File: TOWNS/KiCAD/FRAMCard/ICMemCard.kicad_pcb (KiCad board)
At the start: 2 copper layers, 79.1 x 50.5 mm, 19 parts, among them J1 PCMCIA_Connector, Q1 BC846X, Q2 BC846X, U1 FM18W08-SGTR, U2 FM18W08-SGTR, U3 74AHCT1G32

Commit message: Working on PCB for NX1 PCMCIA frame.
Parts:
- removed the REF** at (139.1, 99.9)
- removed the REF** at (139.1, 51.9)
- added REF**: MountingHole_1.5mm, MountingHole:MountingHole_2.1mm, F.Cu at (68.5, 59.3)
- added REF**: MountingHole_1.5mm, MountingHole:MountingHole_2.1mm, F.Cu at (59.3, 92.8)
- moved U1 9.38 mm to (102.1, 81.2)
- moved D1 8.41 mm to (66.5, 66.3), turned to 90 degrees
- moved D2 6.64 mm to (66.5, 71.6), turned to 90 degrees
- moved U2 2.57 mm to (109.9, 63.3)
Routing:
- net /A12: track 54.1 -> 75.8 mm
- net GND: track 555.9 -> 538.5 mm, vias 3 -> 4
- net Vcc: track 282.4 -> 270.0 mm
- net /A6: track 70.7 -> 59.8 mm, vias 0 -> 2
- net /D0: track 39.5 -> 49.6 mm
- net /D1: track 41.6 -> 51.7 mm
- net Net-(D1-Pad1): track 18.6 -> 28.6 mm
- net /D7: track 62.5 -> 72.5 mm
- net /~WE~orWP: track 130.8 -> 140.5 mm
- net /A11: track 82.5 -> 92.0 mm
- net /D2: track 44.8 -> 54.4 mm
- net /D6: track 66.0 -> 75.2 mm
- net /D5: track 70.0 -> 79.1 mm
- net /~OE: track 132.8 -> 141.9 mm
- net /D4: track 74.2 -> 83.0 mm
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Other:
- board size 79.1 x 50.5 mm -> 78.5 x 47.2 mm
- board text added: "FM TOWNS RESCUE BOOT MEMORY CARD Using HIROSE NX1 PCMCIA FRAME by Captain YS http://www.ysflight.com Ver. 20220514"
- board text added: "PCMCIA Connector"
- board text removed: "FM TOWNS RESCUE BOOT MEMORY CARD by Captain YS http://www.ysflight.com Ver. 20220514"
- board text removed: "PCMCIA Connector 95622-003LF"

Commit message: Working on PCB for NX1 PCMCIA frame.
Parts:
- moved U3 11.5 mm to (74.7, 87.8), turned to 270 degrees
- moved REF** 9.12 mm to (68.5, 92.5)
- moved JP1 7.12 mm to (65.5, 84.1)
- moved C1 6.03 mm to (86.4, 89.9)
- moved D1 0.83 mm to (65.7, 66.3)
- moved D2 0.83 mm to (65.7, 71.6)
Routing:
- net GND: track 538.5 -> 377.2 mm
- net Vcc: track 270.0 -> 234.6 mm
- net /Wp: track 95.4 -> 83.6 mm
- net /~WE~orWP: track 140.5 -> 136.2 mm
- net /~WE: track 73.6 -> 75.6 mm
- net Net-(D1-Pad2): track 12.3 -> 14.3 mm
- net Net-(D2-Pad1): track 29.3 -> 31.2 mm
- net /D8: track 91.6 -> 90.1 mm
- net /D9: track 91.4 -> 90.0 mm
- net Net-(D1-Pad1): track 28.6 -> 29.9 mm
- net /D4: track 83.0 -> 81.9 mm
- net /D10: track 90.8 -> 89.8 mm
- net /A4: track 70.2 -> 69.3 mm
- net Net-(D2-Pad2): track 10.8 -> 11.6 mm
- net /D5: track 79.1 -> 78.3 mm
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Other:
- board text added: "Mounting Hole 2.1mm X 4.1mm Oval"
- board text removed: "Write_Unprotect"

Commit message: Working on PCB for NX1 PCMCIA frame.
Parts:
- moved D1 1.33 mm to (64.4, 66.3)
- moved D2 1.33 mm to (64.4, 71.6)
- moved U3 0.18 mm to (74.7, 87.6)
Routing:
- net Vcc: track 234.6 -> 212.6 mm, vias 4 -> 6
- net Net-(D2-Pad1): track 31.2 -> 35.4 mm
- net Net-(D1-Pad2): track 14.3 -> 16.6 mm
- net Net-(D2-Pad2): track 11.6 -> 13.8 mm
- net Net-(D1-Pad1): track 29.9 -> 29.5 mm, vias 0 -> 2

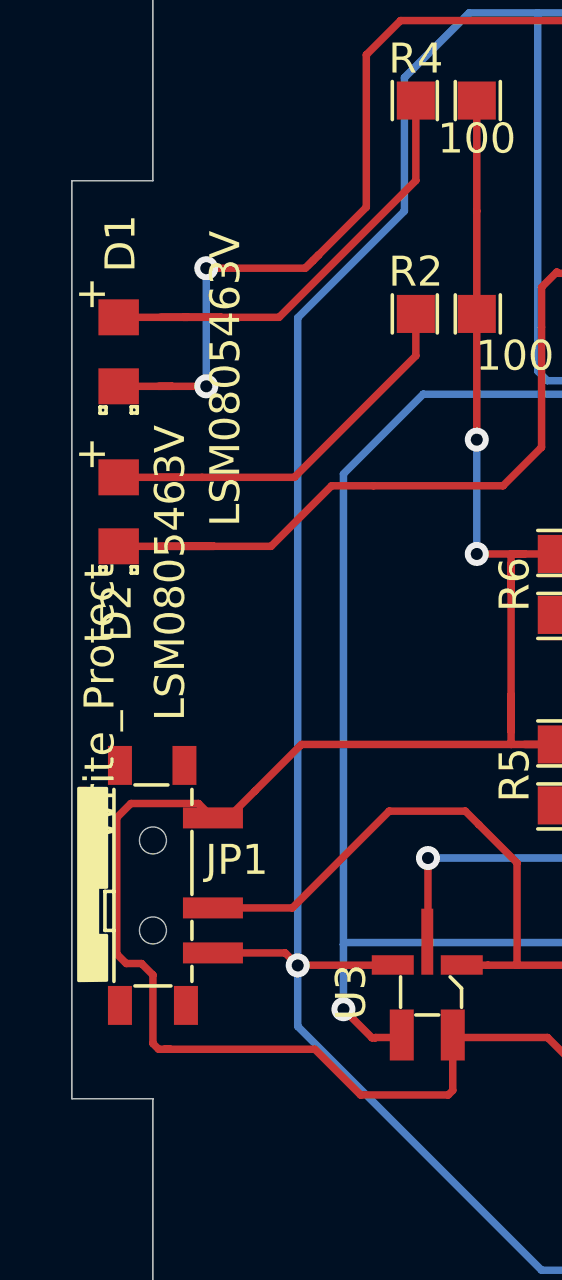
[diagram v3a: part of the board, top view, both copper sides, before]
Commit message: Added fillet
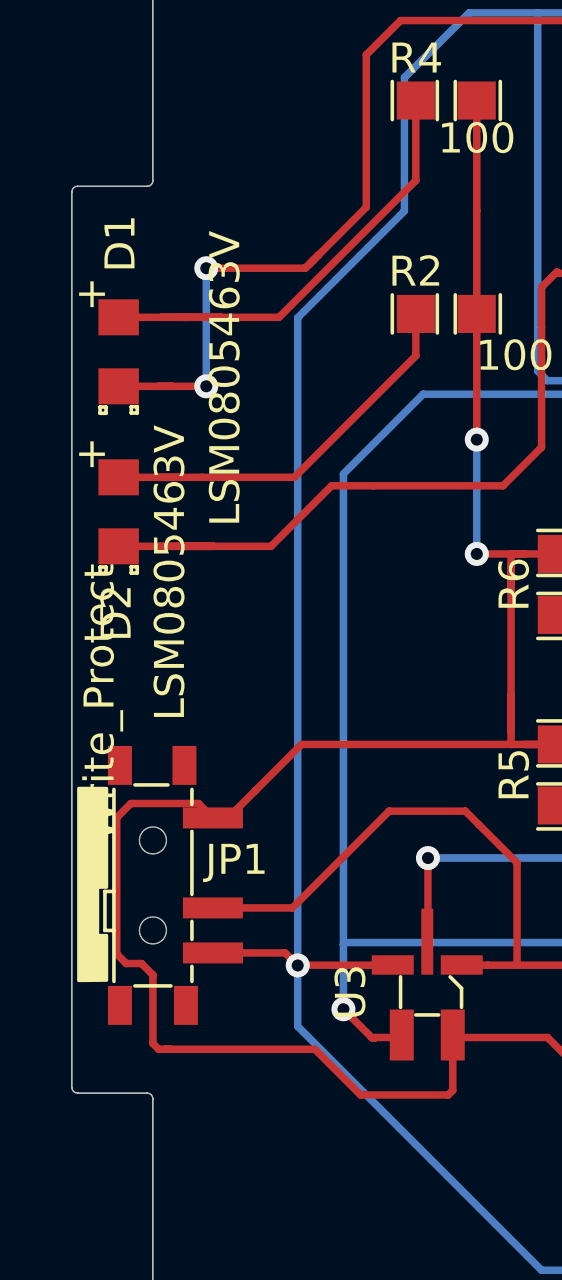
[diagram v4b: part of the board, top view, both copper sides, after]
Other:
- outline, holes or cut-outs redrawn

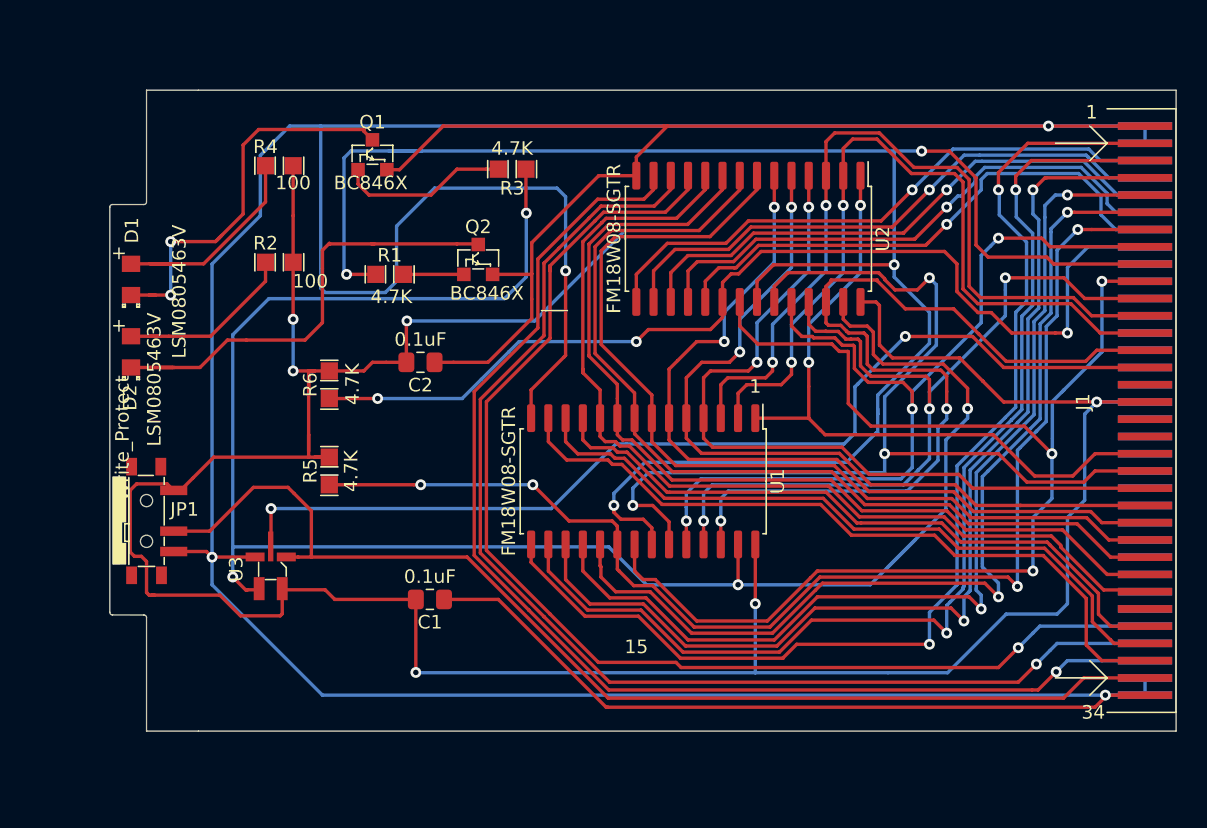
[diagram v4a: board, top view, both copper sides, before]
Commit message: Use 74LS32 instead of 1-CH OR gate.  Easier soldering.
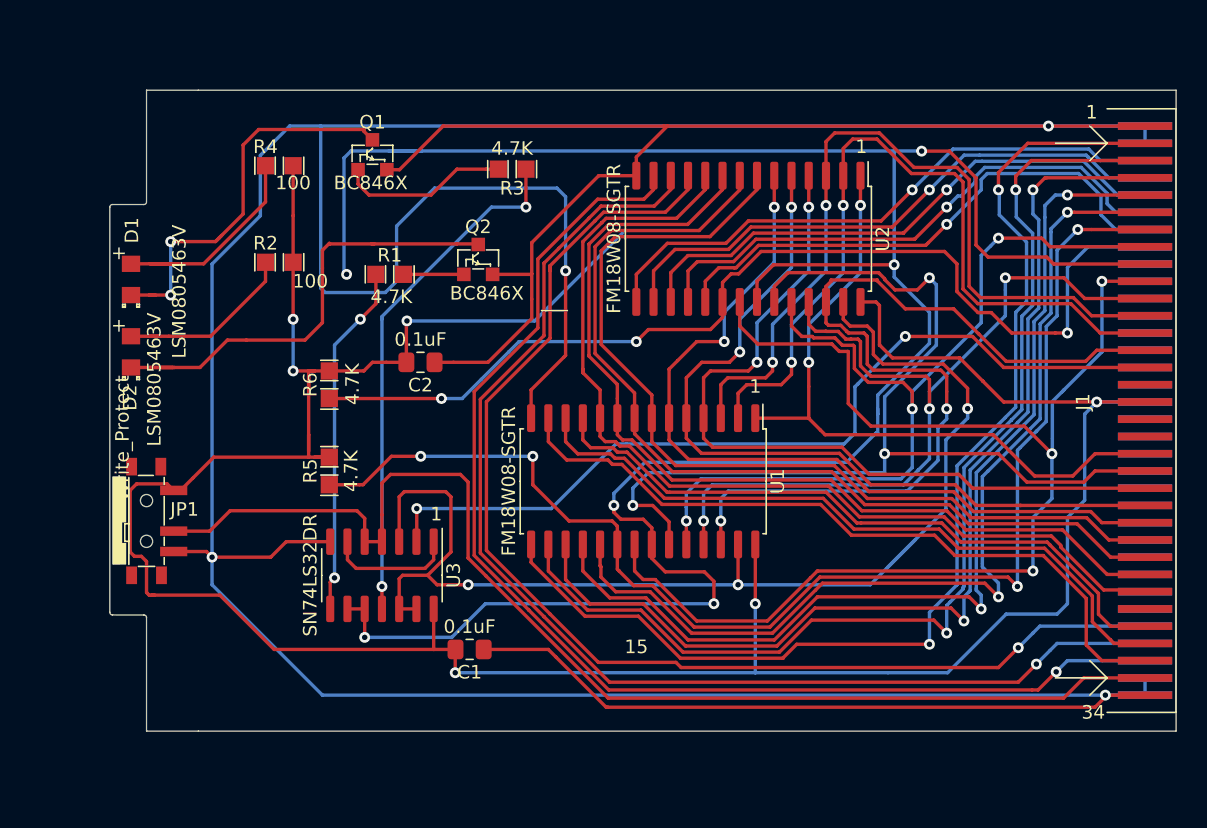
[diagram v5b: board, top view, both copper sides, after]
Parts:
- U3: value 74AHCT1G32 -> SN74LS32DR; footprint PCMCIA:SOT353_Easy -> Package_SO:SOIC-14_3.9x8.7mm_P1.27mm
- moved U3 8.20 mm to (82.9, 88.1)
- moved C1 4.70 mm to (89.3, 93.5)
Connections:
- R1 pad 2: /~OE -> Net-(R1-Pad2)
- R3 pad 2: /~WE~orWP -> Net-(R3-Pad2)
- U3 pad 1: /Wp -> /WPorWP
- U3 pad 3: GND -> /~WE~orWP
- U3 pad 4: /~WE~orWP -> /Wp
- U3 pad 5: Vcc -> /Wp
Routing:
- net /~WE~orWP: track 136.5 -> 89.3 mm, vias 4 -> 3
- net Net-(R3-Pad2): track 0.00 -> 38.3 mm, vias 0 -> 2
- net /~OE: track 141.9 -> 177.8 mm, vias 4 -> 6
- net Net-(R1-Pad2): track 0.00 -> 26.0 mm, vias 0 -> 2
- net /~WE: track 75.6 -> 64.3 mm
- net /WPorWP: track 0.00 -> 9.54 mm
- net /Wp: track 84.0 -> 89.4 mm
- net /~CE1: track 91.8 -> 94.7 mm
- net Vcc: track 212.6 -> 210.8 mm
- net GND: track 377.2 -> 378.6 mm

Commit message: Cleaning up PCB
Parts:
- JP1: value Write_Protect -> WP
- moved R5 2.67 mm to (74.4, 80.4)
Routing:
- net /~OE: track 177.8 -> 117.3 mm, vias 6 -> 5
- net Vcc: track 210.8 -> 204.9 mm
- net /~CE1: track 94.7 -> 99.6 mm
- net /Wp: track 89.4 -> 87.1 mm
- net /A11: track 92.0 -> 94.0 mm
- net /D7: track 72.5 -> 74.4 mm
- net /D6: track 74.7 -> 76.5 mm
- net /D5: track 78.3 -> 79.4 mm
- net /D3: track 84.3 -> 85.3 mm
- net /D4: track 81.9 -> 83.0 mm
- net /~WE~orWP: track 89.3 -> 88.3 mm
- net /D9: track 90.0 -> 89.3 mm
- net /D10: track 89.8 -> 89.3 mm
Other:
- board text added: "FM TOWNS RESCUE BOOT MEMORY CARD Using HIROSE NX1 PCMCIA FRAME by Captain YS http://www.ysflight.com Ver. 20220520"
- board text removed: "FM TOWNS RESCUE BOOT MEMORY CARD Using HIROSE NX1 PCMCIA FRAME by Captain YS http://www.ysflight.com Ver. 20220514"

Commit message: Cleaning up PCB
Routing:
- net GND: track 378.2 -> 347.4 mm
- net /~OE: track 117.3 -> 103.5 mm
- net /A14: track 68.0 -> 65.4 mm
- net /D11: track 43.7 -> 45.7 mm
- net /D12: track 42.7 -> 44.6 mm
- net /A9: track 63.5 -> 61.9 mm
- net /D13: track 41.5 -> 43.1 mm
- net /~WE~orWP: track 88.3 -> 87.2 mm
- net /D14: track 41.1 -> 42.2 mm
- net /A10: track 66.7 -> 65.7 mm
- net /A12: track 75.6 -> 74.6 mm
- net /A8: track 59.2 -> 59.7 mm
- net /A13: track 57.6 -> 58.1 mm

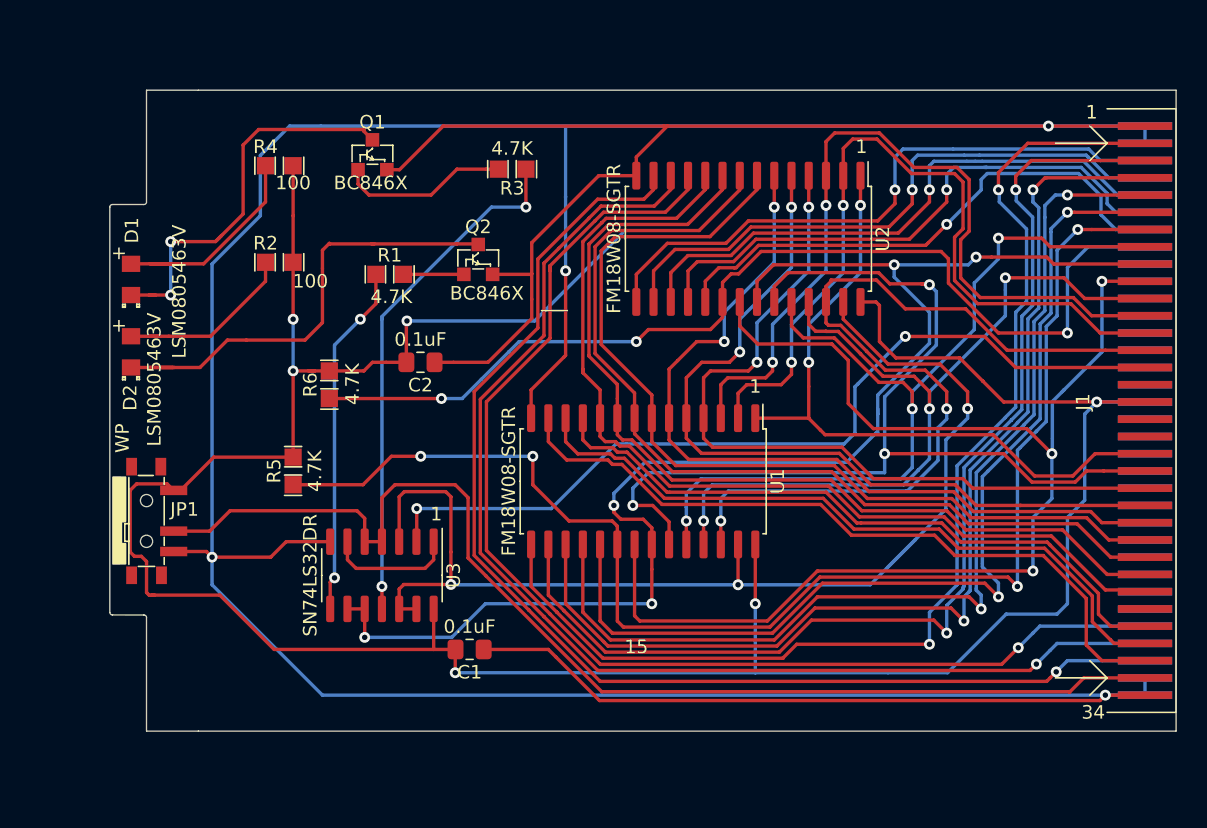
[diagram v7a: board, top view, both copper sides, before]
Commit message: Updating PCB bare version.
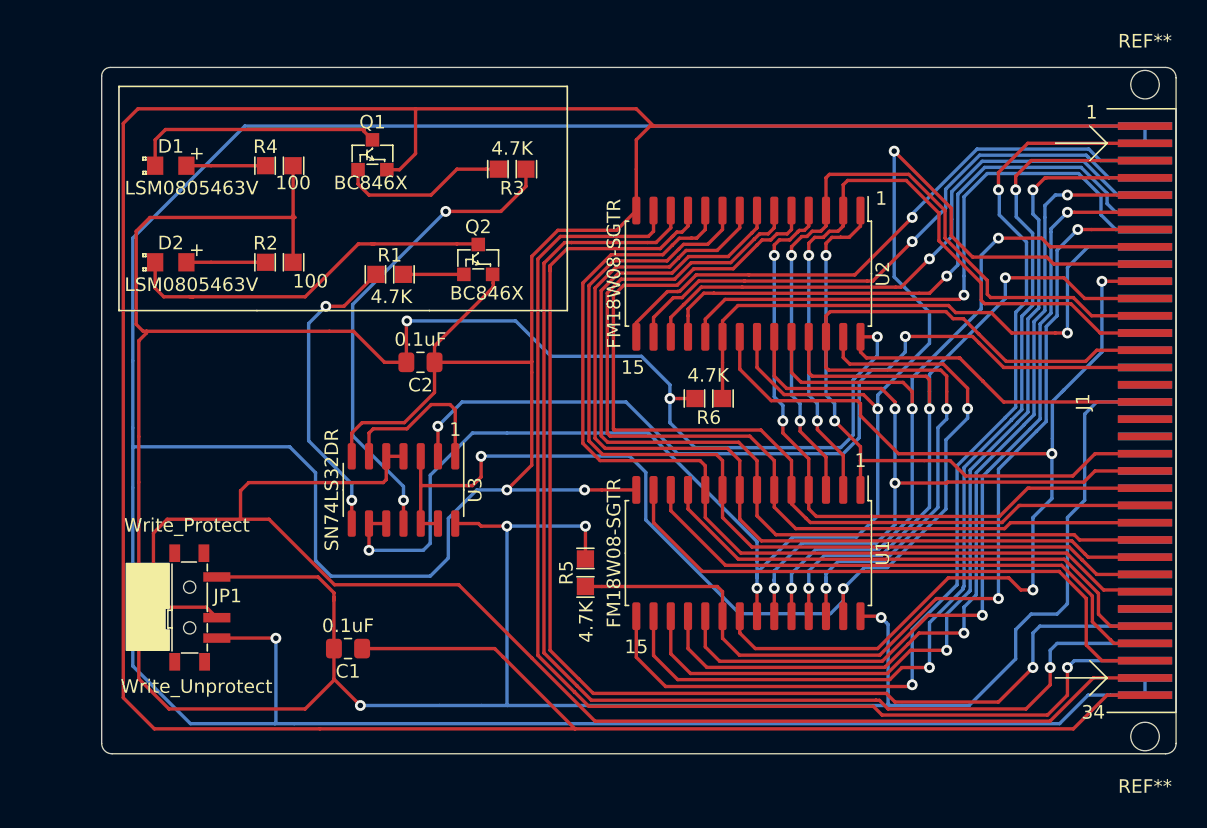
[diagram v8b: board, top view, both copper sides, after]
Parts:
- removed the REF** at (68.5, 59.3)
- removed the REF** at (68.5, 92.5)
- added REF**: MountingHole_1.5mm, MountingHole:MountingHole_2.1mm, F.Cu at (139.1, 99.9)
- added REF**: MountingHole_1.5mm, MountingHole:MountingHole_2.1mm, F.Cu at (139.1, 51.9)
- JP1: value WP -> Write_Protect
- moved R6 30.0 mm to (106.9, 77.0), turned to 180 degrees
- moved R5 22.8 mm to (95.9, 87.9)
- moved U1 9.38 mm to (109.9, 86.4)
- moved C1 8.95 mm to (80.4, 93.5)
- moved D1 8.87 mm to (67.3, 57.9), turned to 0 degrees
- moved D2 7.22 mm to (67.3, 65.0), turned to 0 degrees
- moved JP1 7.12 mm to (68.7, 90.4)
- moved U3 6.48 mm to (84.5, 81.8)
- moved U2 2.57 mm to (109.9, 65.9)
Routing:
- net GND: track 347.4 -> 529.5 mm, vias 4 -> 3
- net Vcc: track 204.8 -> 293.6 mm, vias 6 -> 7
- net /~CE2: track 75.1 -> 43.6 mm, vias 3 -> 1
- net /~CE1: track 99.6 -> 70.8 mm, vias 4 -> 2
- net /A12: track 74.6 -> 54.1 mm
- net /Wp: track 87.1 -> 106.9 mm
- net /~OE: track 103.5 -> 123.2 mm, vias 5 -> 4
- net /D7: track 74.4 -> 62.5 mm
- net /A11: track 93.6 -> 82.5 mm
- net /A6: track 59.7 -> 70.7 mm, vias 2 -> 0
- net Net-(D1-Pad1): track 29.5 -> 18.6 mm, vias 2 -> 0
- net Net-(D1-Pad2): track 16.6 -> 5.83 mm
- net /D6: track 76.5 -> 66.0 mm
- net /D0: track 49.6 -> 39.5 mm
- net /D1: track 51.7 -> 41.6 mm
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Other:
- board size 78.5 x 47.2 mm -> 79.1 x 50.5 mm
- board text added: "FM TOWNS RESCUE BOOT MEMORY CARD by Captain YS http://www.ysflight.com Ver. 20220520"
- board text added: "PCMCIA Connector 95622-003LF"
- board text added: "Write_Unprotect"
- board text removed: "FM TOWNS RESCUE BOOT MEMORY CARD Using HIROSE NX1 PCMCIA FRAME by Captain YS http://www.ysflight.com Ver. 20220520"
- board text removed: "Mounting Hole 2.1mm X 4.1mm Oval"
- board text removed: "PCMCIA Connector"
